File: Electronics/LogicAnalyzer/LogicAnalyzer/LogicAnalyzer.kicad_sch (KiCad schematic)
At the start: 2 parts, among them J1 Conn_02x15_Odd_Even, U1 Pico

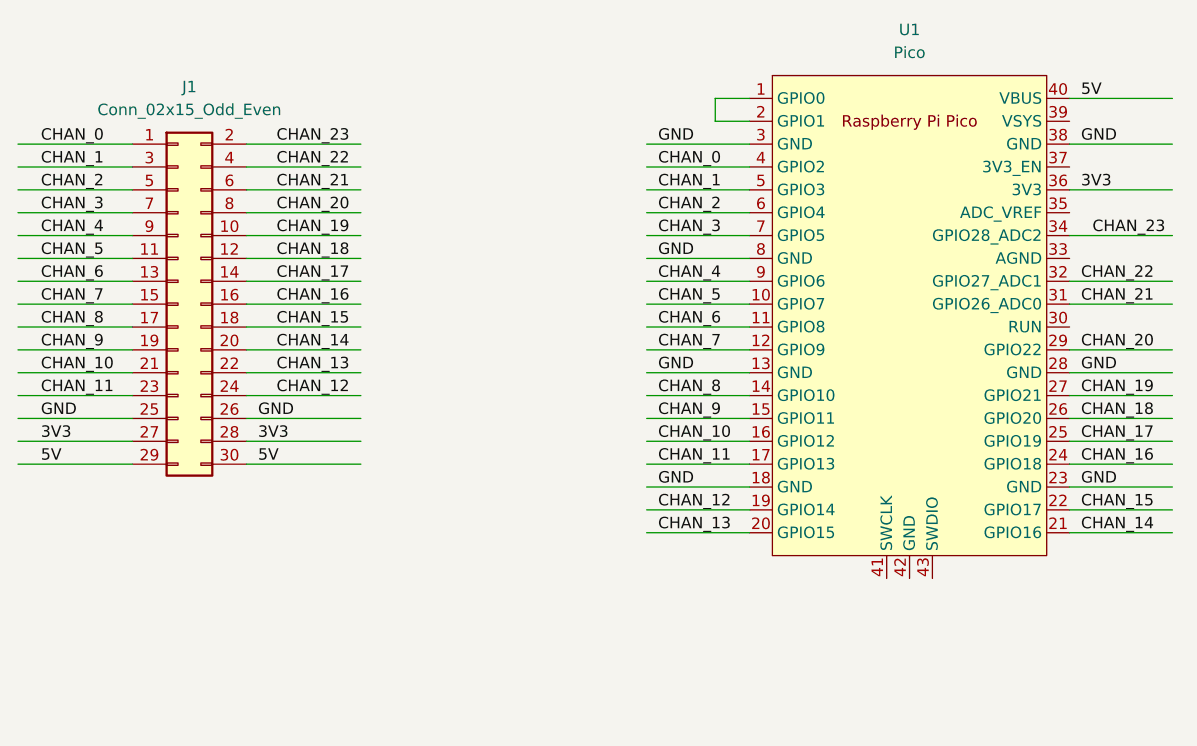
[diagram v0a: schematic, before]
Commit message: New external trigger
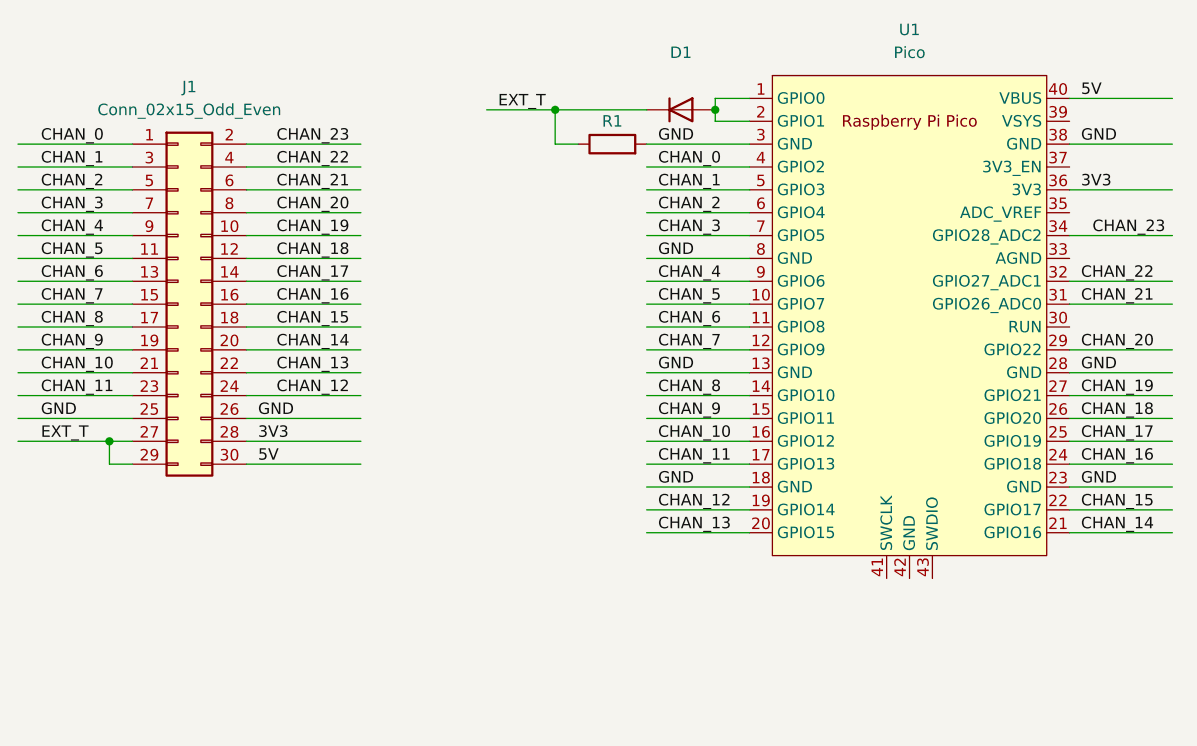
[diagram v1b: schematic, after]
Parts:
- added D1: (no value), symbol Diode:LL4148
- added R1: (no value), symbol Device:R
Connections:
- net 3V3: no longer J1.27 (Pin_27)
- net 5V: no longer J1.29 (Pin_29)
- net GND: now also R1.2
- net at U1.1 (GPIO0), U1.2 (GPIO1): now also D1.2 (A)
- new net EXT_T: D1.1 (K), J1.27 (Pin_27), J1.29 (Pin_29), R1.1

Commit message: Version 4.0
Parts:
- added J2: Conn_01x03, Connector_PinSocket_2.54mm:PinSocket_1x03_P2.54mm_Horizontal, symbol Connector_Generic:Conn_01x03
- added J3: Conn_01x03, Connector_PinHeader_2.54mm:PinHeader_1x03_P2.54mm_Horizontal, symbol Connector_Generic:Conn_01x03
- D1: value (none) -> LL4148; footprint (none) -> Diode_SMD:D_MiniMELF
- R1: value (none) -> 100k; footprint (none) -> Resistor_SMD:R_0603_1608Metric
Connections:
- net GND: now also J2.3 (Pin_3), J3.3 (Pin_3)
- net EXT_CHAIN: now reaches D1.2 (A), U1.1 (GPIO0), U1.2 (GPIO1)
- net EXT_CHAIN: now also J2.1 (Pin_1), J3.1 (Pin_1)
- no-connect marks 0 -> 10
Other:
- moved on the sheet: D1
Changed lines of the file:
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@@
   (junction (at 156.21 71.12) (diameter 0) (color 0 0 0 0)
   )
+  (junction (at 153.67 71.12) (diameter 0) (color 0 0 0 0)
+  )
+  (no_connect (at 96.52 135.89))
+  (no_connect (at 161.29 135.89))
+  (no_connect (at 195.58 95.25))
+  (no_connect (at 195.58 72.39))
+  (no_connect (at 195.58 77.47))
+  (no_connect (at 195.58 82.55))
+  (no_connect (at 195.58 87.63))
+  (no_connect (at 180.34 123.19))
+  (no_connect (at 177.8 123.19))
+  (no_connect (at 175.26 123.19))
   (wire (pts (xy 148.59 95.25) (xy 160.02 95.25))
     (stroke (width 0) (type default) (color 0 0 0 0))
   )
+  (wire (pts (xy 151.13 71.12) (xy 153.67 71.12))
+    (stroke (width 0) (type default) (color 0 0 0 0))
+  )
   (wire (pts (xy 104.14 110.49) (xy 116.84 110.49))
     (stroke (width 0) (type default) (color 0 0 0 0))
@@
     (stroke (width 0) (type default) (color 0 0 0 0))
   )
-  (wire (pts (xy 138.43 71.12) (xy 148.59 71.12))
+  (wire (pts (xy 138.43 71.12) (xy 143.51 71.12))
     (stroke (width 0) (type default) (color 0 0 0 0))
   )
@@
     (stroke (width 0) (type default) (color 0 0 0 0))
   )
-  (wire (pts (xy 130.81 71.12) (xy 138.43 71.12))
-    (stroke (width 0) (type default) (color 0 0 0 0))
-  )
   (wire (pts (xy 116.84 100.33) (xy 104.14 100.33))
     (stroke (width 0) (type default) (color 0 0 0 0))
   )
+  (wire (pts (xy 128.27 71.12) (xy 138.43 71.12))
+    (stroke (width 0) (type default) (color 0 0 0 0))
+  )
   (wire (pts (xy 195.58 115.57) (xy 207.01 115.57))
     (stroke (width 0) (type default) (color 0 0 0 0))
@@
     (stroke (width 0) (type default) (color 0 0 0 0))
   )
+  (wire (pts (xy 149.86 138.43) (xy 161.29 138.43))
+    (stroke (width 0) (type default) (color 0 0 0 0))
+  )
   (wire (pts (xy 148.59 100.33) (xy 160.02 100.33))
     (stroke (width 0) (type default) (color 0 0 0 0))
@@
     (stroke (width 0) (type default) (color 0 0 0 0))
   )
-  (wire (pts (xy 160.02 69.85) (xy 156.21 69.85))
+  (wire (pts (xy 156.21 69.85) (xy 160.02 69.85))
+    (stroke (width 0) (type default) (color 0 0 0 0))
+  )
+  (wire (pts (xy 128.27 63.5) (xy 153.67 63.5))
     (stroke (width 0) (type default) (color 0 0 0 0))
   )
@@
     (stroke (width 0) (type default) (color 0 0 0 0))
   )
+  (wire (pts (xy 153.67 63.5) (xy 153.67 71.12))
+    (stroke (width 0) (type default) (color 0 0 0 0))
+  )
   (wire (pts (xy 195.58 74.93) (xy 207.01 74.93))
     (stroke (width 0) (type default) (color 0 0 0 0))
@@
     (stroke (width 0) (type default) (color 0 0 0 0))
   )
+  (wire (pts (xy 85.09 138.43) (xy 96.52 138.43))
+    (stroke (width 0) (type default) (color 0 0 0 0))
+  )
   (wire (pts (xy 116.84 92.71) (xy 104.14 92.71))
     (stroke (width 0) (type default) (color 0 0 0 0))
@@
     (stroke (width 0) (type default) (color 0 0 0 0))
   )
+  (wire (pts (xy 149.86 133.35) (xy 161.29 133.35))
+    (stroke (width 0) (type default) (color 0 0 0 0))
+  )
   (wire (pts (xy 140.97 74.93) (xy 138.43 74.93))
     (stroke (width 0) (type default) (color 0 0 0 0))
@@
     (stroke (width 0) (type default) (color 0 0 0 0))
   )
+  (wire (pts (xy 153.67 71.12) (xy 156.21 71.12))
+    (stroke (width 0) (type default) (color 0 0 0 0))
+  )
   (wire (pts (xy 116.84 85.09) (xy 104.14 85.09))
     (stroke (width 0) (type default) (color 0 0 0 0))
   )
+  (wire (pts (xy 85.09 133.35) (xy 96.52 133.35))
+    (stroke (width 0) (type default) (color 0 0 0 0))
+  )
   (wire (pts (xy 195.58 113.03) (xy 207.01 113.03))
     (stroke (width 0) (type default) (color 0 0 0 0))
@@
     (effects (font (size 1.27 1.27)) (justify left bottom))
   )
-  (label "EXT_T" (at 132.08 71.12 0)
+  (label "EXT_T" (at 129.54 71.12 0)
     (effects (font (size 1.27 1.27)) (justify left bottom))
   )
@@
     (effects (font (size 1.27 1.27)) (justify left bottom))
   )
+  (label "GND" (at 151.13 138.43 0)
+    (effects (font (size 1.27 1.27)) (justify left bottom))
+  )
   (label "GND" (at 149.86 113.03 0)
     (effects (font (size 1.27 1.27)) (justify left bottom))
@@
     (effects (font (size 1.27 1.27)) (justify left bottom))
   )
+  (label "EXT_CHAIN" (at 130.81 63.5 0)
+    (effects (font (size 1.27 1.27)) (justify left bottom))
+  )
   (label "CHAN_18" (at 115.57 87.63 180)
     (effects (font (size 1.27 1.27)) (justify right bottom))
@@
     (effects (font (size 1.27 1.27)) (justify left bottom))
   )
+  (label "EXT_CHAIN" (at 151.13 133.35 0)
+    (effects (font (size 1.27 1.27)) (justify left bottom))
+  )
   (label "GND" (at 196.85 74.93 0)
     (effects (font (size 1.27 1.27)) (justify left bottom))
@@
     (effects (font (size 1.27 1.27)) (justify left bottom))
   )
+  (label "EXT_CHAIN" (at 86.36 133.35 0)
+    (effects (font (size 1.27 1.27)) (justify left bottom))
+  )
   (label "GND" (at 149.86 74.93 0)
     (effects (font (size 1.27 1.27)) (justify left bottom))
@@
   (label "CHAN_21" (at 115.57 80.01 180)
     (effects (font (size 1.27 1.27)) (justify right bottom))
+  )
+  (label "GND" (at 86.36 138.43 0)
+    (effects (font (size 1.27 1.27)) (justify left bottom))
   )
   (label "CHAN_0" (at 81.28 74.93 0)
@@
     (pin "9")
   )
-  (symbol (lib_id "Diode:LL4148") (at 152.4 71.12 0) (unit 1)
+  (symbol (lib_id "Diode:LL4148") (at 147.32 71.12 0) (unit 1)
     (in_bom yes) (on_board yes) (fields_autoplaced)
-    (property "Reference" "D1" (id 0) (at 152.4 64.77 0))
-    (property "Value" "" (id 1) (at 152.4 67.31 0))
-    (property "Footprint" "" (id 2) (at 152.4 75.565 0)
-      (effects (font (size 1.27 1.27)) hide)
-    )
-    (property "Datasheet" "http://www.vishay.com/docs/85557/ll4148.pdf" (id 3) (at 152.4 71.12 0)
+    (property "Reference" "D1" (id 0) (at 147.32 64.77 0))
+    (property "Value" "LL4148" (id 1) (at 147.32 67.31 0))
+    (property "Footprint" "Diode_SMD:D_MiniMELF" (id 2) (at 147.32 75.565 0)
+      (effects (font (size 1.27 1.27)) hide)
+    )
+    (property "Datasheet" "http://www.vishay.com/docs/85557/ll4148.pdf" (id 3) (at 147.32 71.12 0)
       (effects (font (size 1.27 1.27)) hide)
     )
     (pin "1")
     (pin "2")
+  )
+  (symbol (lib_id "Connector_Generic:Conn_01x03") (at 166.37 135.89 0) (unit 1)
+    (in_bom yes) (on_board yes) (fields_autoplaced)
+    (property "Reference" "J3" (id 0) (at 168.91 134.6199 0)
+      (effects (font (size 1.27 1.27)) (justify left))
+    )
+    (property "Value" "Conn_01x03" (id 1) (at 168.91 137.1599 0)
+      (effects (font (size 1.27 1.27)) (justify left))
+    )
+    (property "Footprint" "Connector_PinHeader_2.54mm:PinHeader_1x03_P2.54mm_Horizontal" (id 2) (at 166.37 135.89 0)
+      (effects (font (size 1.27 1.27)) hide)
+    )
+    (property "Datasheet" "~" (id 3) (at 166.37 135.89 0)
+      (effects (font (size 1.27 1.27)) hide)
+    )
+    (pin "1")
+    (pin "2")
+    (pin "3")
   )
   (symbol (lib_id "Connector_Generic:Conn_02x15_Odd_Even") (at 96.52 92.71 0) (unit 1)
@@
     (in_bom yes) (on_board yes)
     (property "Reference" "R1" (id 0) (at 144.78 72.39 90))
-    (property "Value" "" (id 1) (at 144.78 77.47 90))
-    (property "Footprint" "" (id 2) (at 144.78 76.708 90)
+    (property "Value" "100k" (id 1) (at 144.78 77.47 90))
+    (property "Footprint" "Resistor_SMD:R_0603_1608Metric" (id 2) (at 144.78 76.708 90)
       (effects (font (size 1.27 1.27)) hide)
     )
@@
     (pin "1")
     (pin "2")
+  )
+  (symbol (lib_id "Connector_Generic:Conn_01x03") (at 101.6 135.89 0) (unit 1)
+    (in_bom yes) (on_board yes) (fields_autoplaced)
+    (property "Reference" "J2" (id 0) (at 104.14 134.6199 0)
+      (effects (font (size 1.27 1.27)) (justify left))
+    )
+    (property "Value" "Conn_01x03" (id 1) (at 104.14 137.1599 0)
+      (effects (font (size 1.27 1.27)) (justify left))
+    )
+    (property "Footprint" "Connector_PinSocket_2.54mm:PinSocket_1x03_P2.54mm_Horizontal" (id 2) (at 101.6 135.89 0)
+      (effects (font (size 1.27 1.27)) hide)
+    )
+    (property "Datasheet" "~" (id 3) (at 101.6 135.89 0)
+      (effects (font (size 1.27 1.27)) hide)
+    )
+    (pin "1")
+    (pin "2")
+    (pin "3")
   )
   (sheet_instances
@@
       (reference "J1") (unit 1) (value "Conn_02x15_Odd_Even") (footprint "Connector_PinSocket_2.54mm:PinSocket_2x15_P2.54mm_Horizontal")
     )
+    (path "/ff241e45-ad71-468a-af34-530f0c7608e6"
+      (reference "J2") (unit 1) (value "Conn_01x03") (footprint "Connector_PinSocket_2.54mm:PinSocket_1x03_P2.54mm_Horizontal")
+    )
+    (path "/8effd443-b0b6-40d4-943d-96cc25aee3c6"
+      (reference "J3") (unit 1) (value "Conn_01x03") (footprint "Connector_PinHeader_2.54mm:PinHeader_1x03_P2.54mm_Horizontal")
+    )
     (path "/af0af41e-659e-4e99-9b35-33f9dcf2ed42"
